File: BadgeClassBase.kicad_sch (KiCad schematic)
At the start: 29 parts, among them J1 RP2040_SWD, SW1 RESET, SW2 BOOTSEL, U1 W25Q32JVZP, U2 RP2040, Y1 12.0MHz

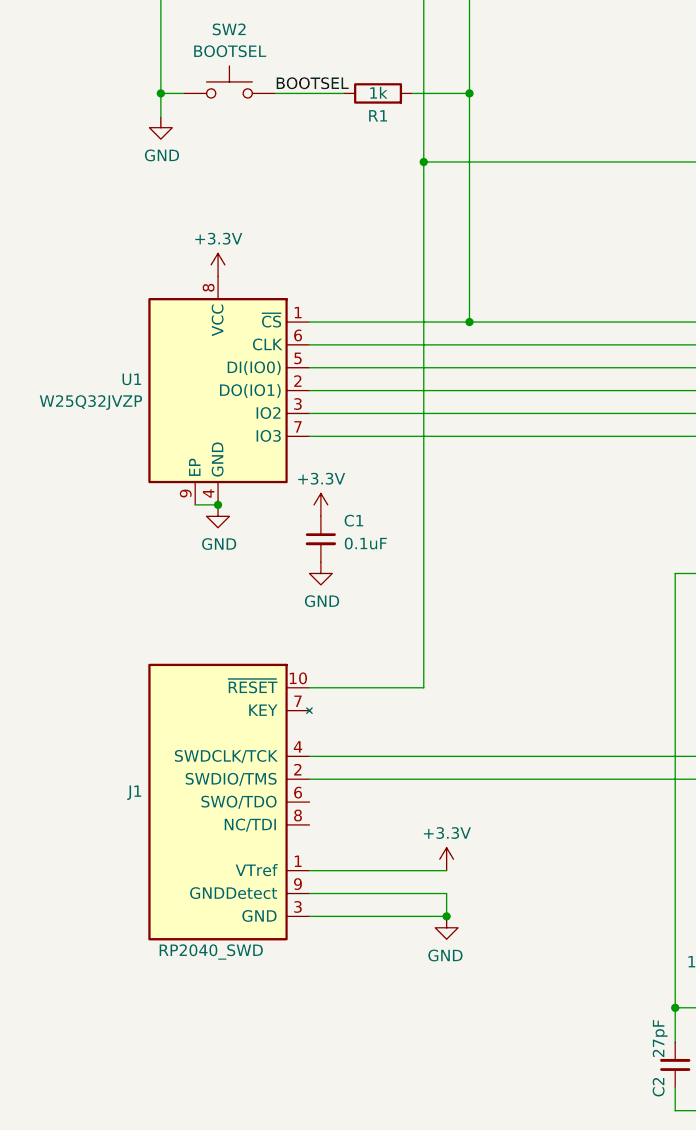
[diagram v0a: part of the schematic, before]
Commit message: Added paw-connect library. Changed SWD to use the 6 contact pinout using the paw-connect symbol (RevB)
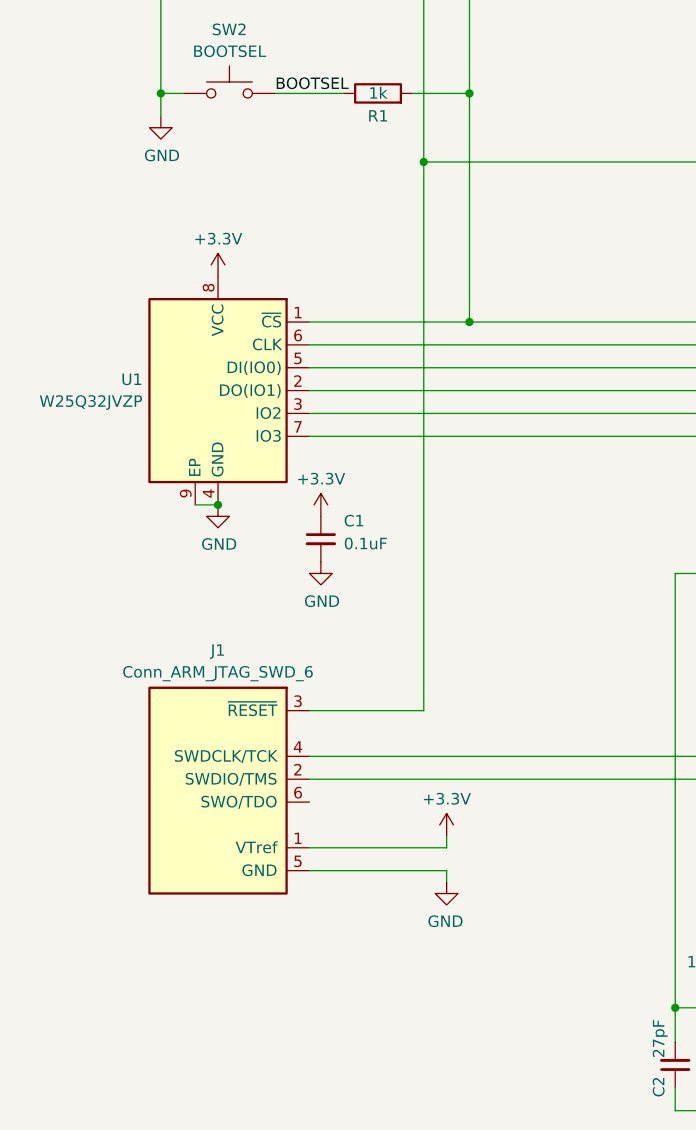
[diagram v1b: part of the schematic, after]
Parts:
- removed J1: RP2040_SWD, symbol Cheetah:Conn_ARM_JTAG_SWD_10
- added J1: Conn_ARM_JTAG_SWD_6, BadgeClass:Paw-Connect_RevB_TC2030-IDC-NL_2x03_P1.27mm_Vertical, symbol BadgeClass:Conn_ARM_JTAG_SWD_6
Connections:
- net +3.3V: now also J1.1 (VTref)
- net GND: now also J1.5 (GND)
- net RP2040_SWCLK: now also J1.4 (SWDCLK/TCK)
- net RP2040_SWDIO: now also J1.2 (SWDIO/TMS)
- net ~{RESET}: now also J1.3 (~{RESET})
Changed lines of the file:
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@@
   (junction (at 144.78 39.37) (diameter 0) (color 0 0 0 0)
   )
-  (junction (at 91.44 147.32) (diameter 0) (color 0 0 0 0)
-  )
   (junction (at 140.97 54.61) (diameter 0) (color 0 0 0 0)
   )
@@
     (stroke (width 0) (type default))
   )
-  (wire (pts (xy 91.44 147.32) (xy 91.44 144.78))
+  (wire (pts (xy 91.44 143.51) (xy 91.44 142.24))
     (stroke (width 0) (type default))
   )
@@
     (stroke (width 0) (type default))
   )
-  (wire (pts (xy 76.2 121.92) (xy 88.9 121.92))
+  (wire (pts (xy 76.2 124.46) (xy 88.9 124.46))
     (stroke (width 0) (type default))
   )
@@
     (stroke (width 0) (type default))
   )
+  (wire (pts (xy 91.44 139.7) (xy 76.2 139.7))
+    (stroke (width 0) (type default))
+  )
   (wire (pts (xy 127 119.38) (xy 148.59 119.38))
     (stroke (width 0) (type default))
@@
     (stroke (width 0) (type default))
   )
-  (wire (pts (xy 88.9 121.92) (xy 88.9 63.5))
+  (wire (pts (xy 88.9 124.46) (xy 88.9 63.5))
     (stroke (width 0) (type default))
   )
@@
     (stroke (width 0) (type default))
   )
-  (wire (pts (xy 91.44 144.78) (xy 76.2 144.78))
+  (wire (pts (xy 91.44 142.24) (xy 76.2 142.24))
     (stroke (width 0) (type default))
   )
@@
     (stroke (width 0) (type default))
   )
-  (wire (pts (xy 76.2 142.24) (xy 91.44 142.24))
+  (wire (pts (xy 91.44 139.7) (xy 91.44 138.43))
     (stroke (width 0) (type default))
   )
@@
   )
   (wire (pts (xy 199.39 127) (xy 231.14 127))
-    (stroke (width 0) (type default))
-  )
-  (wire (pts (xy 76.2 147.32) (xy 91.44 147.32))
     (stroke (width 0) (type default))
   )
@@
     )
   )
-  (symbol (lib_id "power:GND") (at 91.44 147.32 0) (mirror y) (unit 1)
-    (in_bom yes) (on_board yes) (dnp no)
-    (property "Reference" "#PWR08" (at 91.44 153.67 0)
-      (effects (font (size 1.27 1.27)) hide)
-    )
-    (property "Value" "GND" (at 91.313 151.7142 0)
-      (effects (font (size 1.27 1.27)))
-    )
-    (property "Footprint" "" (at 91.44 147.32 0)
-      (effects (font (size 1.27 1.27)) hide)
-    )
-    (property "Datasheet" "" (at 91.44 147.32 0)
+  (symbol (lib_id "power:GND") (at 91.44 143.51 0) (mirror y) (unit 1)
+    (in_bom yes) (on_board yes) (dnp no)
+    (property "Reference" "#PWR08" (at 91.44 149.86 0)
+      (effects (font (size 1.27 1.27)) hide)
+    )
+    (property "Value" "GND" (at 91.313 147.9042 0)
+      (effects (font (size 1.27 1.27)))
+    )
+    (property "Footprint" "" (at 91.44 143.51 0)
+      (effects (font (size 1.27 1.27)) hide)
+    )
+    (property "Datasheet" "" (at 91.44 143.51 0)
       (effects (font (size 1.27 1.27)) hide)
     )
@@
     )
   )
-  (symbol (lib_id "power:+3.3V") (at 91.44 142.24 0) (unit 1)
+  (symbol (lib_id "power:+3.3V") (at 91.44 138.43 0) (unit 1)
     (in_bom yes) (on_board yes) (dnp no) (fields_autoplaced)
-    (property "Reference" "#PWR07" (at 91.44 146.05 0)
-      (effects (font (size 1.27 1.27)) hide)
-    )
-    (property "Value" "+3.3V" (at 91.44 138.1069 0)
-      (effects (font (size 1.27 1.27)))
-    )
-    (property "Footprint" "" (at 91.44 142.24 0)
-      (effects (font (size 1.27 1.27)) hide)
-    )
-    (property "Datasheet" "" (at 91.44 142.24 0)
+    (property "Reference" "#PWR07" (at 91.44 142.24 0)
+      (effects (font (size 1.27 1.27)) hide)
+    )
+    (property "Value" "+3.3V" (at 91.44 134.2969 0)
+      (effects (font (size 1.27 1.27)))
+    )
+    (property "Footprint" "" (at 91.44 138.43 0)
+      (effects (font (size 1.27 1.27)) hide)
+    )
+    (property "Datasheet" "" (at 91.44 138.43 0)
       (effects (font (size 1.27 1.27)) hide)
     )
@@
         (path "/c07ccd48-8f1d-4e52-b569-b8f01305378d"
           (reference "R2") (unit 4)
-        )
-      )
-    )
-  )
-  (symbol (lib_id "Cheetah:Conn_ARM_JTAG_SWD_10") (at 63.5 132.08 0) (mirror y) (unit 1)
-    (in_bom yes) (on_board yes) (dnp no)
-    (property "Reference" "J1" (at 57.658 133.4516 0)
-      (effects (font (size 1.27 1.27)) (justify left))
-    )
-    (property "Value" "RP2040_SWD" (at 71.12 151.13 0)
-      (effects (font (size 1.27 1.27)) (justify left))
-    )
-    (property "Footprint" "" (at 63.5 132.08 0)
-      (effects (font (size 1.27 1.27)) hide)
-    )
-    (property "Datasheet" "http://infocenter.arm.com/help/topic/com.arm.doc.ddi0314h/DDI0314H_coresight_components_trm.pdf" (at 72.39 143.51 90)
-      (effects (font (size 1.27 1.27)) hide)
-    )
-    (pin "1")
-    (pin "10")
-    (pin "2")
-    (pin "3")
-    (pin "4")
-    (pin "5")
-    (pin "6")
-    (pin "7")
-    (pin "8")
-    (pin "9")
-    (instances
-      (project "BadgeClassBase"
-        (path "/c07ccd48-8f1d-4e52-b569-b8f01305378d"
-          (reference "J1") (unit 1)
         )
       )
@@
         )
       )
+    )
+  )
+  (symbol (lib_id "BadgeClass:Conn_ARM_JTAG_SWD_6") (at 63.5 134.62 0) (mirror y) (unit 1)
+    (in_bom yes) (on_board yes) (dnp no) (fields_autoplaced)
+    (property "Reference" "J1" (at 66.04 117.7757 0)
+      (effects (font (size 1.27 1.27)))
+    )
+    (property "Value" "Conn_ARM_JTAG_SWD_6" (at 66.04 120.1999 0)
+      (effects (font (size 1.27 1.27)))
+    )
+    (property "Footprint" "BadgeClass:Paw-Connect_RevB_TC2030-IDC-NL_2x03_P1.27mm_Vertical" (at 63.5 134.62 0)
+      (effects (font (size 1.27 1.27)) hide)
+    )
+    (property "Datasheet" "http://infocenter.arm.com/help/topic/com.arm.doc.ddi0314h/DDI0314H_coresight_components_trm.pdf" (at 72.39 146.05 90)
+      (effects (font (size 1.27 1.27)) hide)
+    )
+    (pin "6")
+    (pin "4")
+    (pin "5")
+    (pin "2")
+    (pin "3")
+    (pin "1")
+    (instances
+      (project "BadgeClassBase"
+        (path "/c07ccd48-8f1d-4e52-b569-b8f01305378d"
+          (reference "J1") (unit 1)
+        )
+      )

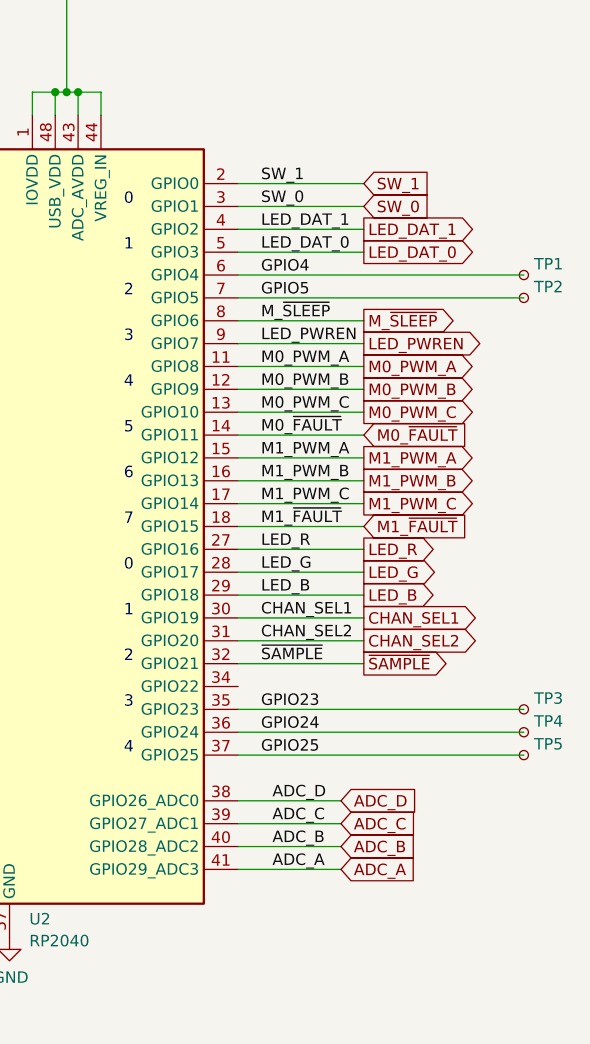
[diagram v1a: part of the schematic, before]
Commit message: Removed old signal names and increased the size of the schematic
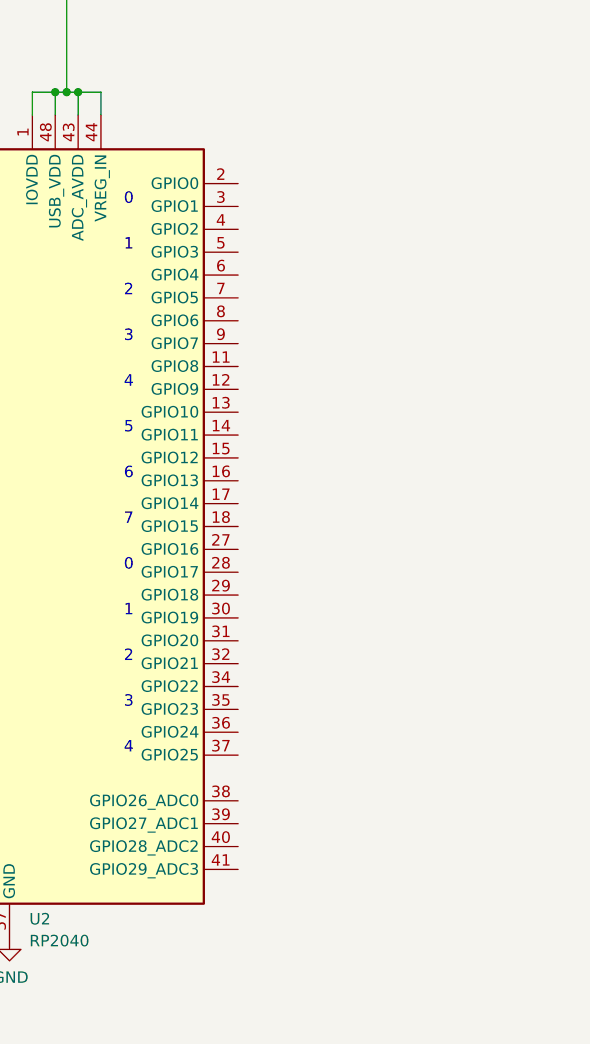
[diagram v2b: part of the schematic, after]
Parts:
- removed TP1, TP2, TP3, TP4, TP5: TestPoint_Small, Cheetah:TestPoint_THTPad_D0.6mm_Drill0.4mm, symbol Connector:TestPoint_Small
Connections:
- net ADC_A: no longer names the net of U2.41 (GPIO29_ADC3)
- net ADC_B: no longer names the net of U2.40 (GPIO28_ADC2)
- net ADC_C: no longer names the net of U2.39 (GPIO27_ADC1)
- net ADC_D: no longer names the net of U2.38 (GPIO26_ADC0)
- net CHAN_SEL1: no longer names the net of U2.30 (GPIO19)
- net CHAN_SEL2: no longer names the net of U2.31 (GPIO20)
- net GPIO23: no longer names the net of U2.35 (GPIO23)
- net GPIO24: no longer names the net of U2.36 (GPIO24)
- net GPIO25: no longer names the net of U2.37 (GPIO25)
- net GPIO4: no longer names the net of U2.6 (GPIO4)
- net GPIO5: no longer names the net of U2.7 (GPIO5)
- net LED_B: no longer names the net of U2.29 (GPIO18)
- net LED_DAT_0: no longer names the net of U2.5 (GPIO3)
- net LED_DAT_1: no longer names the net of U2.4 (GPIO2)
- net LED_G: no longer names the net of U2.28 (GPIO17)
- net LED_PWREN: no longer names the net of U2.9 (GPIO7)
- net LED_R: no longer names the net of U2.27 (GPIO16)
- net M0_PWM_A: no longer names the net of U2.11 (GPIO8)
- net M0_PWM_B: no longer names the net of U2.12 (GPIO9)
- net M0_PWM_C: no longer names the net of U2.13 (GPIO10)
- net M0_~{FAULT}: no longer names the net of U2.14 (GPIO11)
- net M1_PWM_A: no longer names the net of U2.15 (GPIO12)
- net M1_PWM_B: no longer names the net of U2.16 (GPIO13)
- net M1_PWM_C: no longer names the net of U2.17 (GPIO14)
- net M1_~{FAULT}: no longer names the net of U2.18 (GPIO15)
- net M_~{SLEEP}: no longer names the net of U2.8 (GPIO6)
- net SW_0: no longer names the net of U2.3 (GPIO1)
- net SW_1: no longer names the net of U2.2 (GPIO0)
- net ~{SAMPLE}: no longer names the net of U2.32 (GPIO21)
